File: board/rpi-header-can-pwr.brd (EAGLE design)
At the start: 87 x 56.5 mm, 62 parts, among them J1 U.FL, U1 MCP2515, U3 BME280, U4 RFM69HCW, U5 INA219BIDCNT, X1 RJ45-8L21-S, X2 RASPI_BOARD_B+#_E3

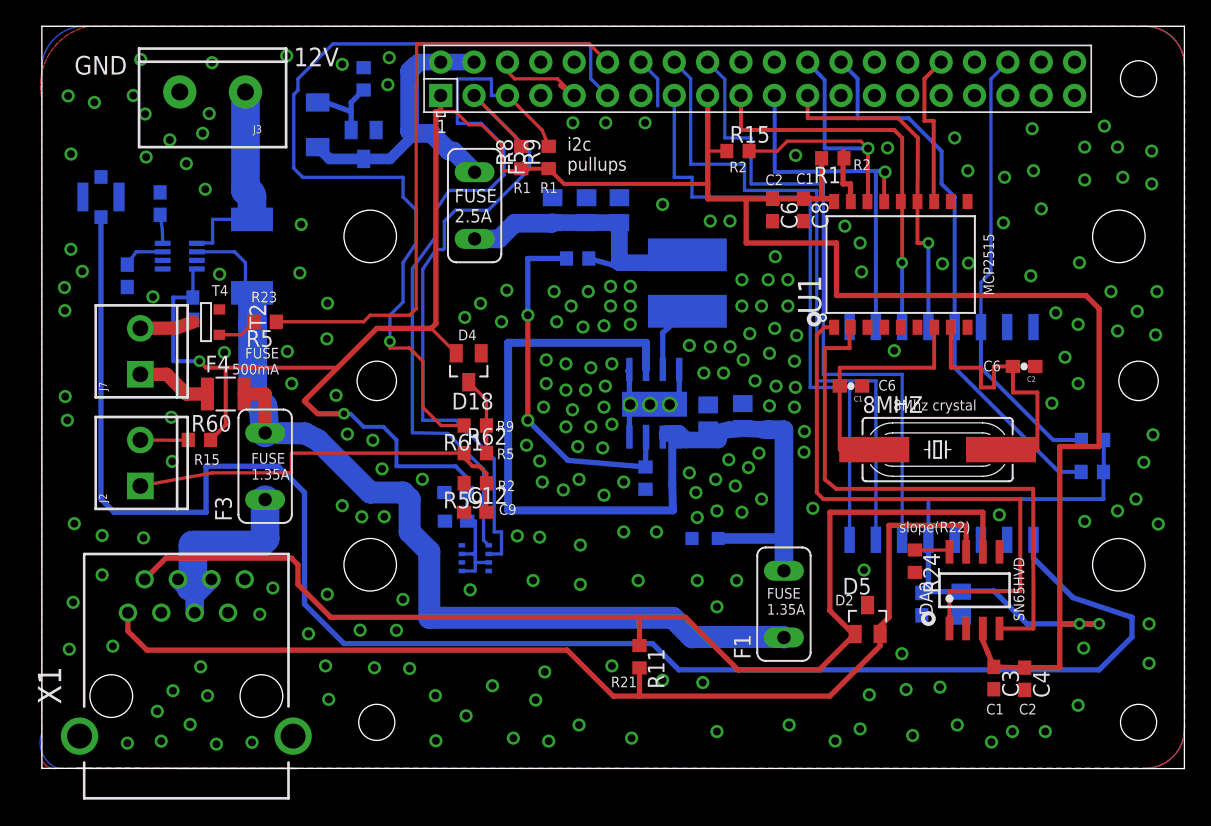
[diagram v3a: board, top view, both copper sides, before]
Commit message: mirror rj45
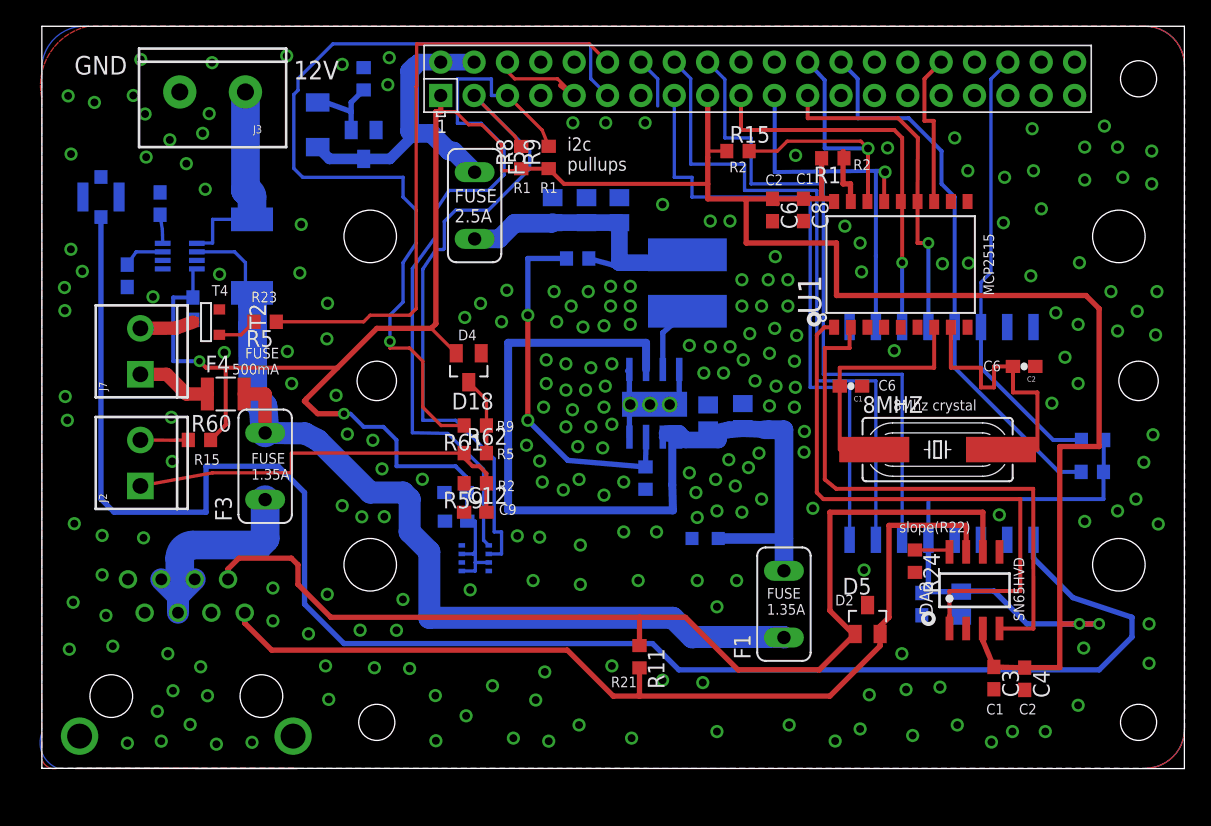
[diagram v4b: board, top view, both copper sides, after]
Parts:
- flipped X1 to the bottom
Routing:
- net CAN_H: track 81.8 -> 72.6 mm
- net CAN_L: track 87.3 -> 81.4 mm
- net CAN_PWR: track 17.1 -> 17.6 mm
- net GND: vias 237 -> 239
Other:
- board text removed: "CAN"
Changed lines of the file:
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@@
 <text x="31.42" y="41.56" size="1.016" layer="121">FUSE
 2.5A</text>
-<text x="19.17" y="53.45" size="1.4224" layer="121">12V</text>
+<text x="19.17" y="52.45" size="1.4224" layer="121">12V</text>
 <text x="2.47" y="52.82" size="1.4224" layer="121">GND</text>
 <text x="33.1" y="33.4" size="0.8128" layer="121" rot="R180">D4</text>
@@
 <text x="11.58" y="23.11" size="0.8128" layer="121">R15</text>
 <text x="2.56" y="20.59" size="1.016" layer="122" rot="MR90">TAMPER</text>
-<text x="22.2" y="52.9" size="0.8128" layer="122" rot="MR180">R5</text>
-<text x="20.2" y="52.6" size="0.8128" layer="122" rot="MR180">D7</text>
+<text x="22.2" y="52.4" size="0.8128" layer="122" rot="MR180">R5</text>
+<text x="20.7" y="46.1" size="0.8128" layer="122" rot="MR180">D7</text>
 <text x="15.94" y="21.98" size="0.8128" layer="121">FUSE
 1.35A</text>
@@
 <circle x="34.87" y="13.92" radius="0.3" width="0.4064" layer="122"/>
 <text x="26.2" y="46.6" size="0.8128" layer="122" rot="MR180">T2</text>
-<text x="19.3" y="55.3" size="1.4224" layer="122" rot="MR180">12V</text>
+<text x="19.3" y="54.3" size="1.4224" layer="122" rot="MR180">12V</text>
 <text x="6.46" y="52.78" size="1.4224" layer="122" rot="MR0">GND</text>
 <text x="47.28" y="40.81" size="0.8128" layer="122" rot="MR0">L1</text>
@@
 ant</text>
 <text x="71.17" y="28.06" size="0.8128" layer="121" rot="R180">8Mhz crystal</text>
-<text x="70.82" y="8.85" size="0.8128" layer="122" rot="MR0">C8</text>
-<text x="67.53" y="8.82" size="0.8128" layer="122" rot="MR0">C1</text>
+<text x="70.82" y="9.35" size="0.8128" layer="122" rot="MR0">C8</text>
+<text x="67.53" y="9.32" size="0.8128" layer="122" rot="MR0">C1</text>
 <text x="83.38" y="24.68" size="0.8128" layer="122" rot="MR0">R2</text>
 <text x="83.44" y="21.9" size="0.8128" layer="122" rot="MR0">R2</text>
@@
 <text x="15.94" y="35.48" size="0.8128" layer="121">R23</text>
 <text x="12.94" y="35.98" size="0.8128" layer="121">T4</text>
-<text x="12.91" y="10.06" size="1.27" layer="122" rot="MR0">CAN</text>
 <text x="63.69" y="28.76" size="0.8128" layer="121">C6</text>
 <text x="71.68" y="30.23" size="0.8128" layer="121">C6</text>
 <text x="18.4" y="37.2" size="0.8128" layer="122" rot="MR90">0.1ohm</text>
-<text x="10.76" y="32.51" size="1.016" layer="122" rot="MR180">C1</text>
+<text x="10.76" y="33.01" size="1.016" layer="122" rot="MR180">C1</text>
 <text x="11.38" y="43.68" size="0.8128" layer="122" rot="MR0">R2</text>
 <text x="6.88" y="34.68" size="0.8128" layer="122" rot="MR0">R2</text>
@@
 <element name="R19" library="microbuilder" package="2512" value="0.1/1% (PT2512FK-070R1L)" x="16" y="39" rot="MR90"/>
 <element name="C18" library="rcl" package="C0603" value="100n" x="11.5" y="35" rot="MR270"/>
-<element name="X1" library="con-tycoelectronics" package="RJ45-SHIELD1" value="RJ45-8L21-S" x="11" y="5.5">
-<attribute name="OC_FARNELL" value="unknown" x="11" y="5.5" size="1.778" layer="27" display="off"/>
-<attribute name="OC_NEWARK" value="unknown" x="11" y="5.5" size="1.778" layer="27" display="off"/>
-<attribute name="MF" value="" x="11" y="5.5" size="1.778" layer="27" display="off"/>
-<attribute name="MPN" value="" x="11" y="5.5" size="1.778" layer="27" display="off"/>
+<element name="X1" library="con-tycoelectronics" package="RJ45-SHIELD1" value="RJ45-8L21-S" x="11" y="5.5" rot="MR0">
+<attribute name="OC_FARNELL" value="unknown" x="11" y="5.5" size="1.778" layer="28" rot="MR0" display="off"/>
+<attribute name="OC_NEWARK" value="unknown" x="11" y="5.5" size="1.778" layer="28" rot="MR0" display="off"/>
+<attribute name="MF" value="" x="11" y="5.5" size="1.778" layer="28" rot="MR0" display="off"/>
+<attribute name="MPN" value="" x="11" y="5.5" size="1.778" layer="28" rot="MR0" display="off"/>
 </element>
 </elements>
@@
 <contactref element="X1" pad="S2"/>
 <via x="4.59" y="14.73" extent="1-16" drill="0.6"/>
-<via x="16.59" y="11.73" extent="1-16" drill="0.6"/>
+<via x="17.59" y="11.23" extent="1-16" drill="0.6"/>
 <via x="17.59" y="13.73" extent="1-16" drill="0.6"/>
 <via x="12.09" y="7.73" extent="1-16" drill="0.6"/>
 <via x="9.74" y="47.85" extent="1-16" drill="0.6"/>
 <via x="12.74" y="49.85" extent="1-16" drill="0.6"/>
+<via x="9.59" y="8.73" extent="1-16" drill="0.6"/>
+<via x="4.88" y="11.64" extent="1-16" drill="0.6"/>
 </signal>
 <signal name="CAN_TX">
@@
 <wire x1="45.5" y1="5.5" x2="43.5" y2="5.5" width="0.4064" layer="1"/>
 <wire x1="43.5" y1="5.5" x2="40" y2="9" width="0.4064" layer="1"/>
-<wire x1="40" y1="9" x2="8" y2="9" width="0.4064" layer="1"/>
+<wire x1="40" y1="9" x2="17.5" y2="9" width="0.4064" layer="1"/>
 <contactref element="R11" pad="2"/>
 <wire x1="45.5" y1="7.65" x2="45.5" y2="5.5" width="0.4064" layer="1"/>
 <contactref element="X1" pad="1"/>
-<wire x1="8" y1="9" x2="6.555" y2="10.445" width="0.4064" layer="1"/>
-<wire x1="6.555" y1="10.445" x2="6.555" y2="11.85" width="0.4064" layer="1"/>
+<wire x1="15.445" y1="11.85" x2="15.445" y2="11.055" width="0.4064" layer="1"/>
+<wire x1="15.445" y1="11.055" x2="17.5" y2="9" width="0.4064" layer="1"/>
 </signal>
 <signal name="CAN_L">
@@
 <wire x1="45.5" y1="9.35" x2="45.5" y2="11.5" width="0.4064" layer="1"/>
 <contactref element="X1" pad="2"/>
-<wire x1="7.825" y1="14.39" x2="9.435" y2="16" width="0.4064" layer="1"/>
-<wire x1="9.435" y1="16" x2="19" y2="16" width="0.4064" layer="1"/>
+<wire x1="15" y1="16" x2="19" y2="16" width="0.4064" layer="1"/>
 <wire x1="19" y1="16" x2="19.5" y2="15.5" width="0.4064" layer="1"/>
 <wire x1="19.5" y1="15.5" x2="19.5" y2="14" width="0.4064" layer="1"/>
 <wire x1="19.5" y1="14" x2="22" y2="11.5" width="0.4064" layer="1"/>
+<wire x1="14.175" y1="14.39" x2="14.175" y2="15.175" width="0.4064" layer="1"/>
+<wire x1="14.175" y1="15.175" x2="15" y2="16" width="0.4064" layer="1"/>
 </signal>
 <signal name="N$17">
@@
 <contactref element="X1" pad="5"/>
 <contactref element="X1" pad="6"/>
-<wire x1="10.365" y1="14.39" x2="11.1275" y2="13.6275" width="1.4224" layer="16"/>
-<wire x1="11.1275" y1="13.6275" x2="11.635" y2="13.12" width="1.4224" layer="16"/>
-<wire x1="11.635" y1="13.12" x2="11.635" y2="11.85" width="1.4224" layer="16"/>
-<wire x1="11.635" y1="13.12" x2="12.905" y2="14.39" width="1.4224" layer="16"/>
 <wire x1="17" y1="20.46" x2="17" y2="17.5" width="2.1844" layer="16"/>
 <wire x1="17" y1="17.5" x2="16.5" y2="17" width="2.1844" layer="16"/>
 <wire x1="16.5" y1="17" x2="11.5" y2="17" width="2.1844" layer="16"/>
-<wire x1="11.5" y1="17" x2="11.5" y2="14" width="2.1844" layer="16"/>
-<wire x1="11.1275" y1="13.6275" x2="11.5" y2="14" width="1.6764" layer="16"/>
+<wire x1="10.365" y1="11.85" x2="10.365" y2="13.12" width="1.6764" layer="16"/>
+<wire x1="10.365" y1="13.12" x2="9.095" y2="14.39" width="1.6764" layer="16"/>
+<wire x1="10.365" y1="13.12" x2="10.6225" y2="13.3775" width="1.6764" layer="16"/>
+<wire x1="10.6225" y1="13.3775" x2="11.635" y2="14.39" width="1.6764" layer="16"/>
+<wire x1="11.5" y1="17" x2="10.5" y2="16" width="2.1844" layer="16" curve="90"/>
+<wire x1="10.5" y1="16" x2="10.5" y2="14" width="2.1844" layer="16"/>
+<wire x1="10.5" y1="14" x2="10.6225" y2="13.8775" width="1.016" layer="16" curve="-90"/>
+<wire x1="10.6225" y1="13.8775" x2="10.6225" y2="13.3775" width="1.016" layer="16"/>
 </signal>
 <signal name="N$5">

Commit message: replace components with ones that has place drawing
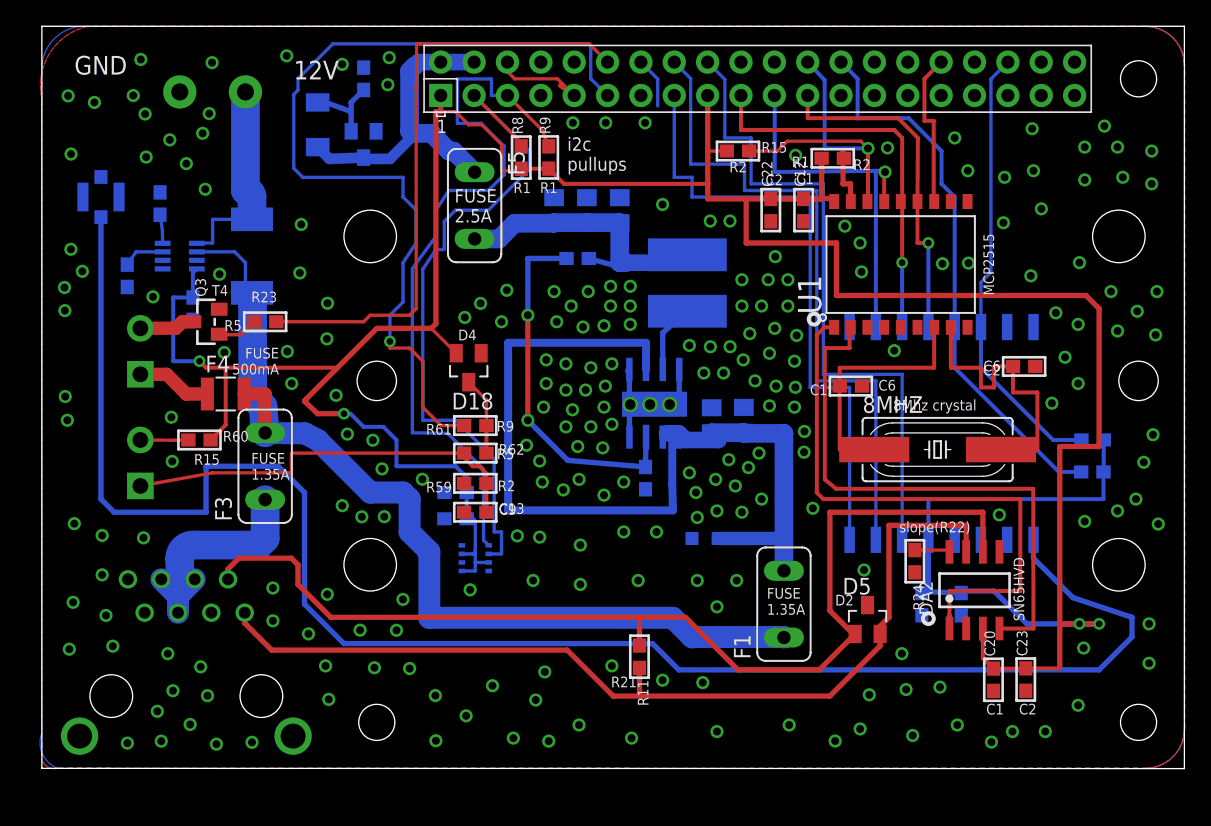
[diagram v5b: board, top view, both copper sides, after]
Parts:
- removed C10: 100n, rcl:C0805
- removed C11, C5, C7: 22uF, rcl:C0805
- removed C18: 100n, rcl:C0603
- removed C9: 4,7u, rcl:C0805
- removed J3: (no value), SparkFun-Connectors:SCREWTERMINAL-5MM-2
- removed T2: (no value), zetex:SOT-23
- added C13: 10nF, microbuilder:0603
- added C19, C20: 100n, microbuilder:0603
- added C21, C22, C23: 1u, microbuilder:0603
- added J4: (no value), SparkFun-Connectors:SCREWTERMINAL-5MM-2
- added Q3: (no value), microbuilder:SOT23-WIDE
- C1, C2: device SparkFun-Capacitors:0603-CAP -> microbuilder:0603
- C12: value 10nF -> 100n; device eagle-ltspice:C0603 -> microbuilder:0603
- C14: value 1u -> 22uF; device rcl:C0603 -> microbuilder:0805
- C15, C8: value 100n -> 22uF; device rcl:C0603 -> microbuilder:0805
- C16: device microbuilder:0603-NO -> microbuilder:0603
- C17: device microbuilder:0805-NO -> microbuilder:0603
- C3: device rcl:C0603 -> microbuilder:0603
- C4: value 1u -> 4,7u; device rcl:C0603 -> microbuilder:0805
- C6: value 1u -> 100n; device rcl:C0603 -> microbuilder:0805
- D3: value BC846 -> (none); device transistor:SOT23 -> microbuilder:SOT23-WIDE
- R1, R11, R14, R15, R17, R2, R24, R3, R4, R5, R59, R60, R61, R62: device rcl:R0603 -> microbuilder:0603
- R12, R13: value 10K -> 1K
- R8, R9: device resistor:R0603 -> microbuilder:0603
- moved C3 67.2 mm to (11.5, 35.0), flipped to the bottom
- moved C12 34.0 mm to (58.0, 42.5), turned to 90 degrees
- moved C4 30.9 mm to (51.0, 26.5), flipped to the bottom, turned to 90 degrees
- moved C15 26.8 mm to (44.0, 42.5), turned to 90 degrees
- moved C14 22.8 mm to (39.0, 42.5), turned to 90 degrees
- moved C8 16.5 mm to (41.5, 42.5), flipped to the bottom, turned to 90 degrees
- moved C6 16.1 mm to (53.5, 26.5), flipped to the bottom, turned to 90 degrees
- flipped J2 to the bottom
- flipped J7 to the bottom
- renumbered R6 to R7
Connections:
- net +12V: now also C4.1, C6.1; no longer C10.1, C9.1
- net +3V3: now also C12.2, C19.2, C20.2, C21.2, C22.2, C23.2; no longer C14.1, C15.1, C18.1, C4.1, C6.1, C8.1
- net GND: now also C13.1, C19.1, C20.1, C21.1, C22.1, C23.1, J4.1, Q3.2; no longer C10.2, C11.2, C18.2, C5.2, C7.2, C9.2, J3.2, T2.2
- net N$11: now also C13.2; no longer C12.2
- net N$12: now also Q3.1; no longer T2.3
- net N$14: now also Q3.3; no longer T2.1
- net N$8: now also C14.1, C15.1, C8.1; no longer C11.1, C5.1, C7.1
- net PRE_SENSE_12V: now also J4.2; no longer J3.1
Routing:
- net +12V: track 75.9 -> 73.9 mm
- net +3V3: track 250.8 -> 250.1 mm
- net N$8: track 22.7 -> 23.2 mm

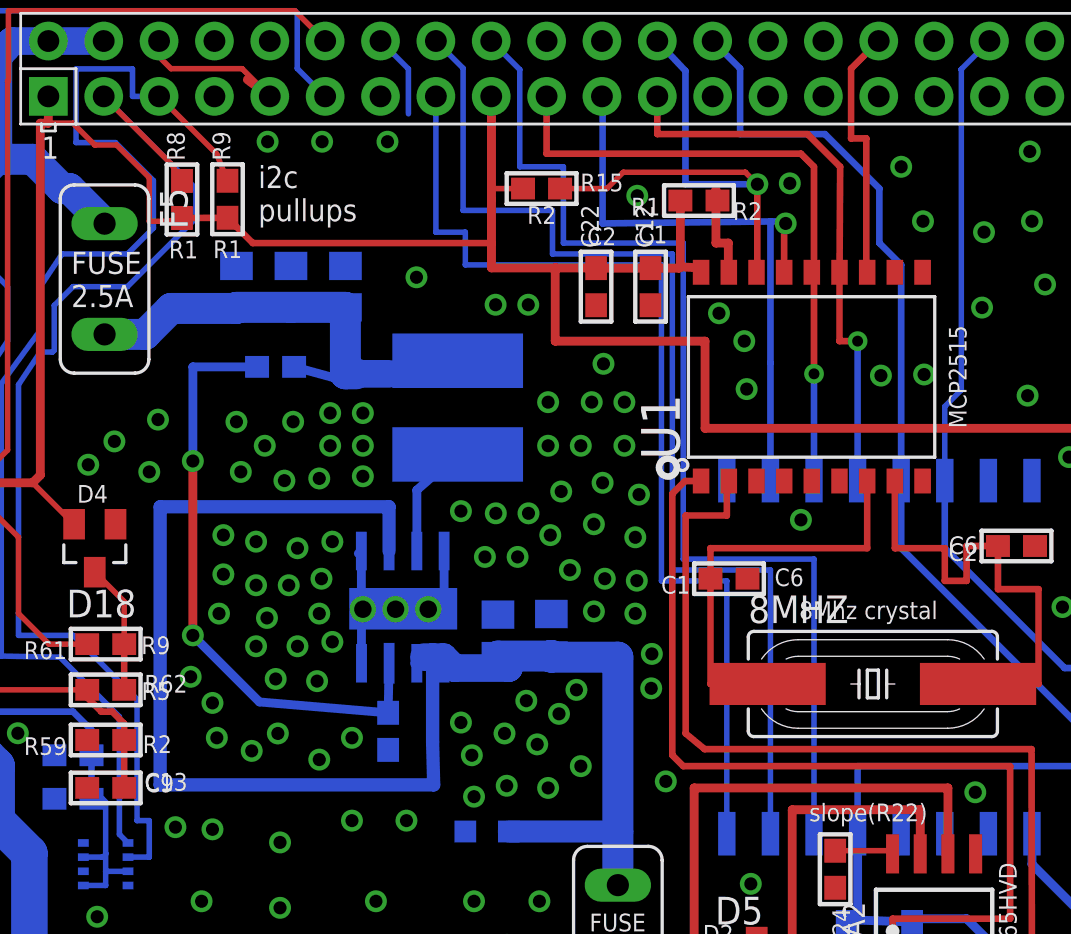
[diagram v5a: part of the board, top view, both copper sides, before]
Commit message: MCP2515 increase pad size
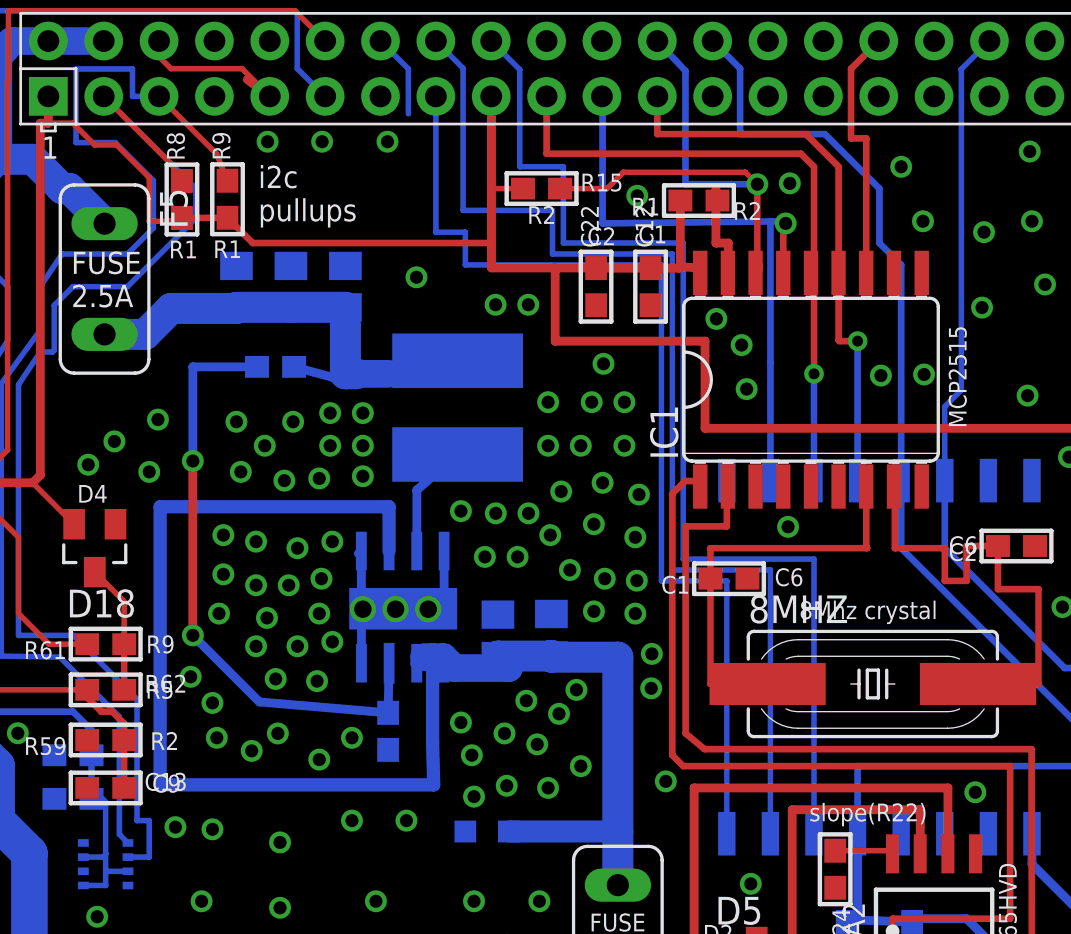
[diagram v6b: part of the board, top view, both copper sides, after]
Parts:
- removed U1: MCP2515, SparkFun-DigitalIC:SO-18W
- added IC1: MCP2515-E/SO, mcp2515:SO18L
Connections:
- net +3V3: now also IC1.18; no longer U1.18
- net CAN_CS: now also IC1.16; no longer U1.16
- net CAN_INT: now also IC1.12; no longer U1.12
- net CAN_RX: now also IC1.2; no longer U1.2
- net CAN_TX: now also IC1.1; no longer U1.1
- net GND: now also IC1.9; no longer U1.9
- net MISO: now also IC1.15; no longer U1.15
- net MOSI: now also IC1.14; no longer U1.14
- net N$2: now also IC1.8; no longer U1.8
- net N$3: now also IC1.7; no longer U1.7
- net RS: now also IC1.17; no longer U1.17
- net SCK: now also IC1.13; no longer U1.13
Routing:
- net CAN_CS: track 24.1 -> 24.6 mm
